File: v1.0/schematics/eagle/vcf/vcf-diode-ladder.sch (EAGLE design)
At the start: 42 parts, among them IC1 TL072P, J1 WAVE IN, J2 CUTOFF CV IN, J3 WAVE OUT, Q1 2N3417, Q2 2N3417, Q3 2N3417, Q4 2N3417, Q5 2N3906

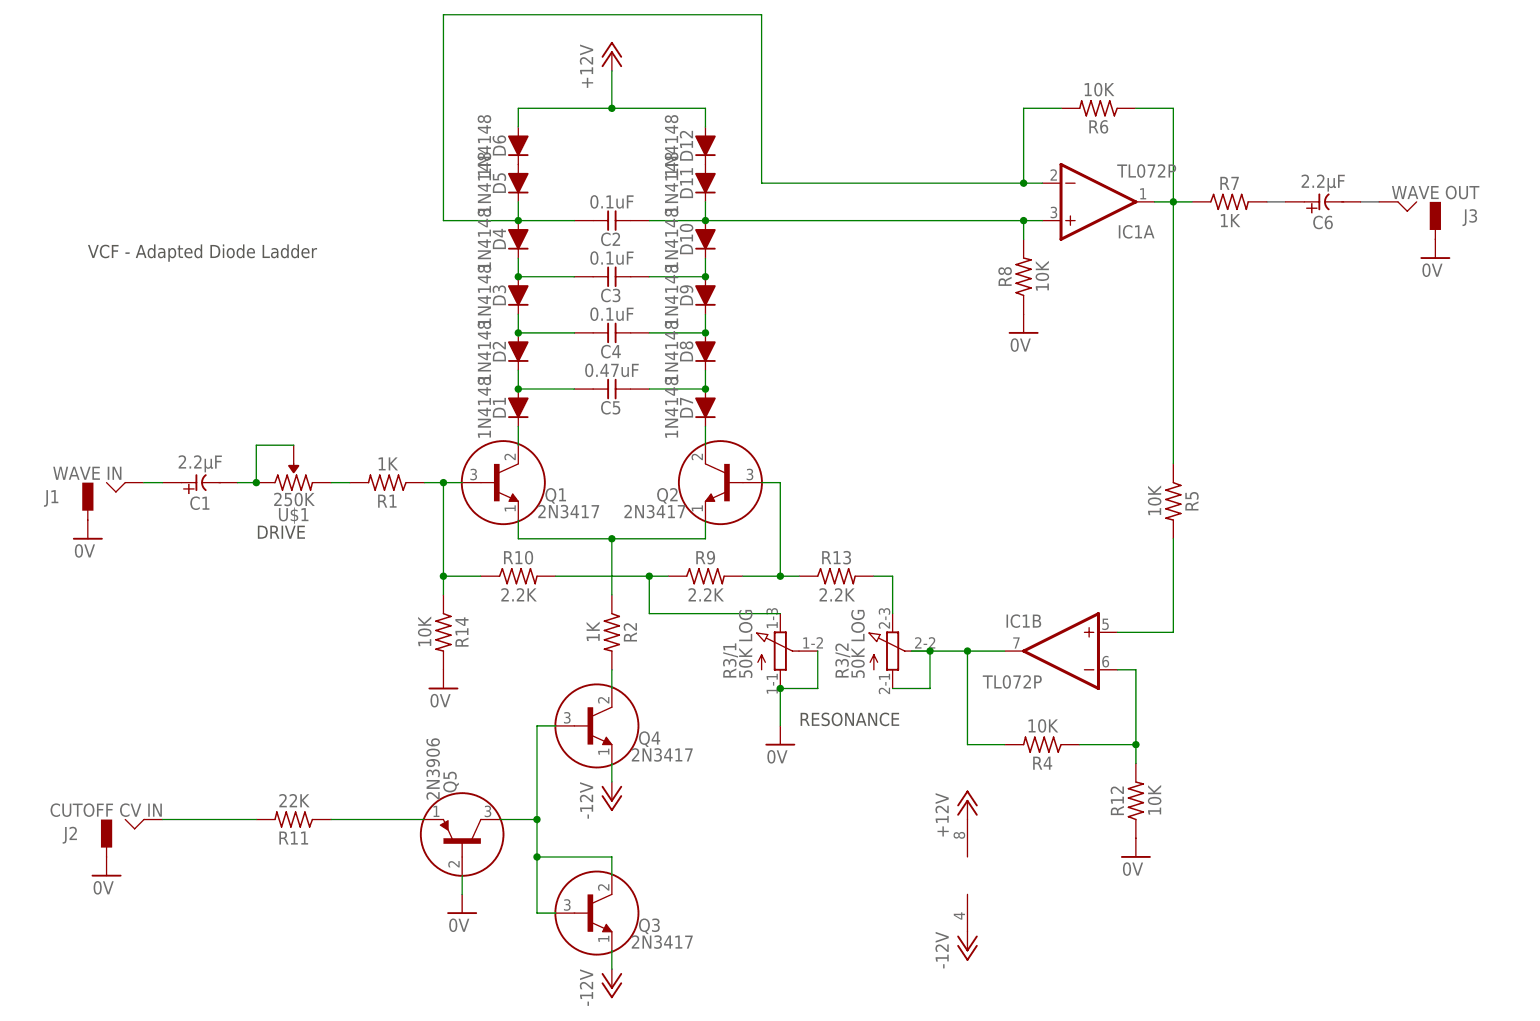
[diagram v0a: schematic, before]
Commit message: Updated vco with correct pot values Updated vcf with new values and added in manual CV control.
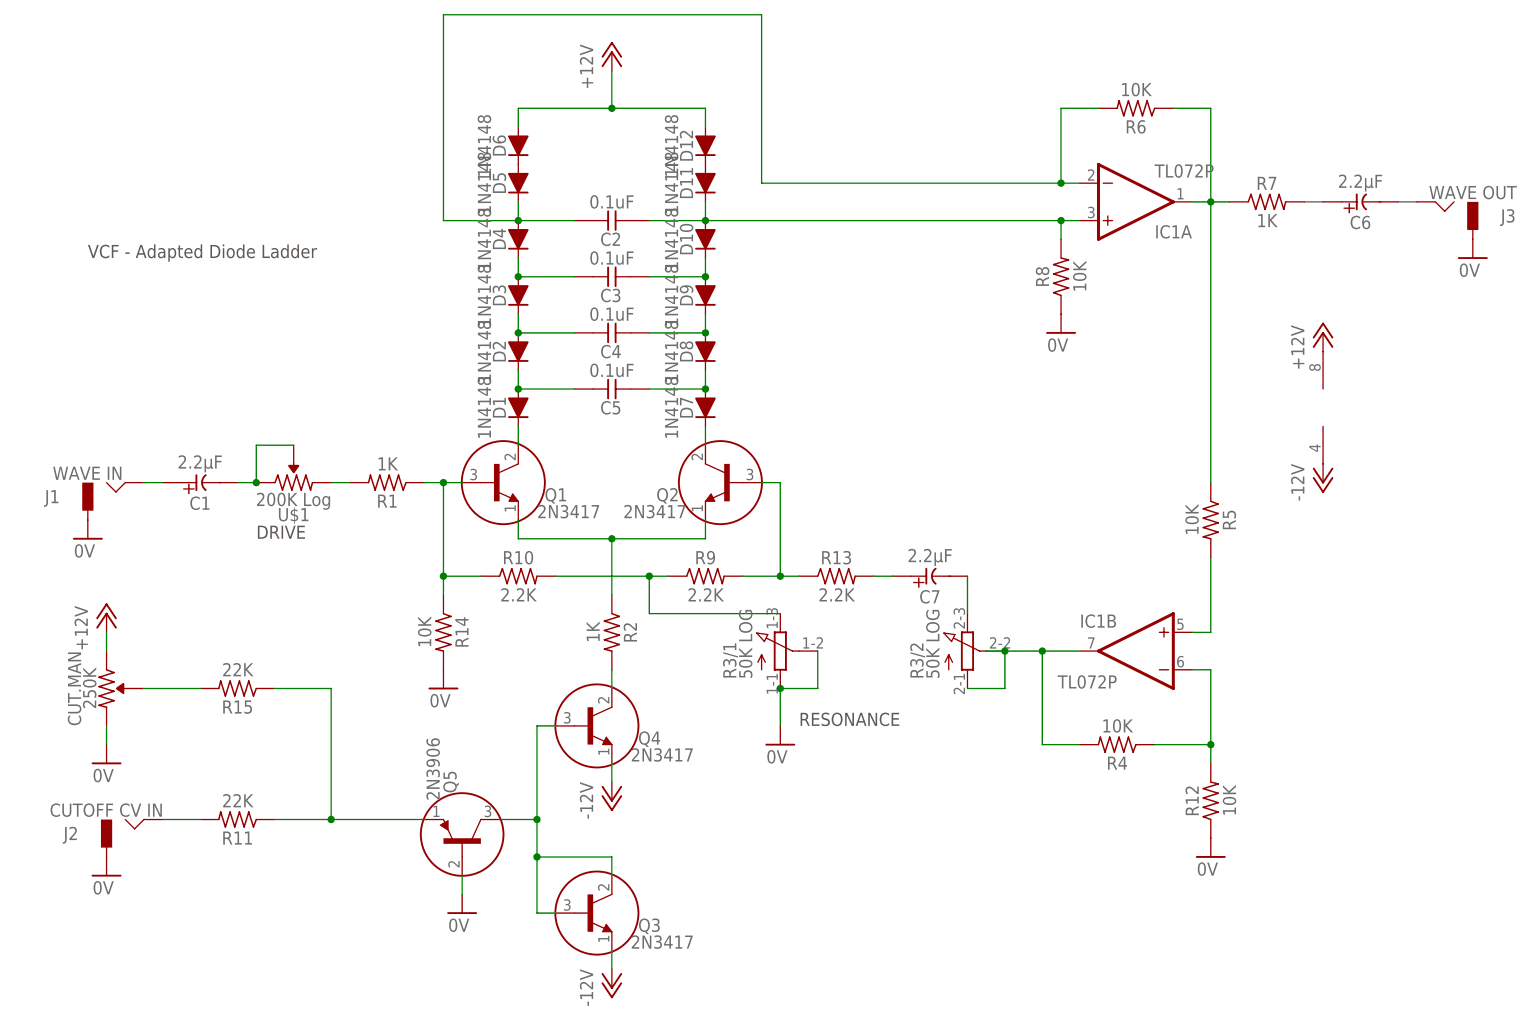
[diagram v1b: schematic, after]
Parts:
- added C7: 2.2μF, _common:CE-USE2-5
- added CUT.MAN: 250K, _common:R-VAR
- added R15: 22K, _common:R0309/10
- C5: value 0.47uF -> 0.1uF
- U$1: value 250K -> 200K Log
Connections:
- new net N$6: CUT.MAN.P$1, R15.2
- new net N$7: C7.-, R3/2.E
- net +12V: now also CUT.MAN.1
- net 0V: now also CUT.MAN.2
- net N$12: now also R15.1
- net N$18: now also C7.+; no longer R3/2.E
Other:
- moved on the sheet: C6, IC1A, IC1B, J3, R11, R12, R3/2, R4, R5, R6, R7, R8

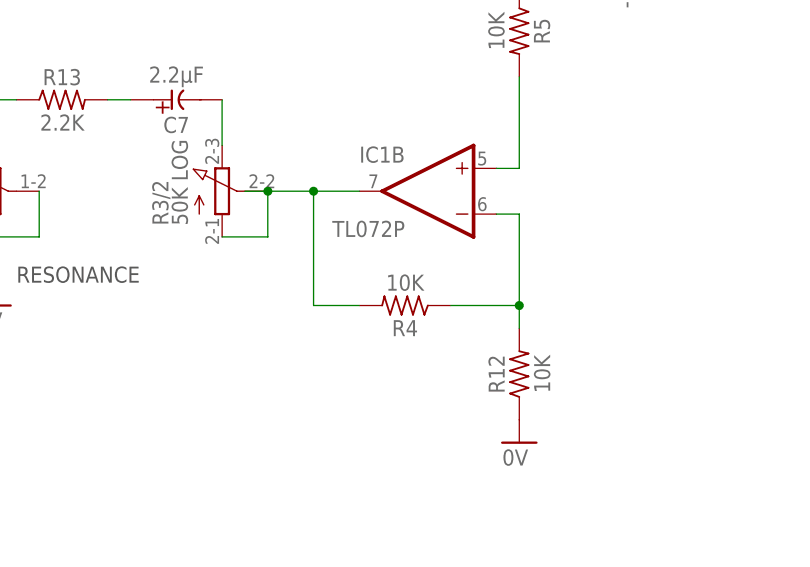
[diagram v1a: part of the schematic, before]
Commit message: updated vcf resonance amp r val
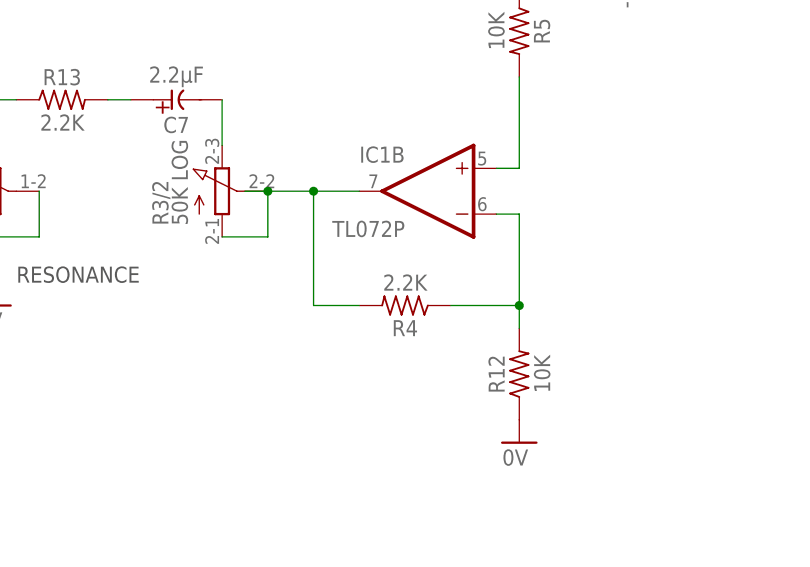
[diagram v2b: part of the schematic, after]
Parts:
- R4: value 10K -> 2.2K
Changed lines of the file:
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@@
 <part name="GND1" library="supply1" deviceset="0V" device=""/>
 <part name="R3" library="pot" deviceset="3RP/1610G" device="" value="50K LOG"/>
-<part name="R4" library="_common" deviceset="R" device="0309/10" value="10K"/>
+<part name="R4" library="_common" deviceset="R" device="0309/10" value="2.2K"/>
 <part name="R5" library="_common" deviceset="R" device="0309/10" value="10K"/>
 <part name="R12" library="_common" deviceset="R" device="0309/10" value="10K"/>

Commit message: Updated VCF
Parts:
- R4: value 2.2K -> 10K
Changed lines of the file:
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@@
 <part name="GND1" library="supply1" deviceset="0V" device=""/>
 <part name="R3" library="pot" deviceset="3RP/1610G" device="" value="50K LOG"/>
-<part name="R4" library="_common" deviceset="R" device="0309/10" value="2.2K"/>
+<part name="R4" library="_common" deviceset="R" device="0309/10" value="10K"/>
 <part name="R5" library="_common" deviceset="R" device="0309/10" value="10K"/>
 <part name="R12" library="_common" deviceset="R" device="0309/10" value="10K"/>

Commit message: Added VCF ATT
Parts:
- added ATT: 250K (lin), _common:R-VAR
- CUT.MAN: value 250K -> 250K (lin)
- R3: value 50K LOG -> 50K (log)
- U$1: value 200K Log -> 200K (log)
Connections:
- new net N$31: ATT.1, ATT.P$1, R11.2
- net N$4: now also ATT.2; no longer R11.2
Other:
- note added: "Updated: 2013-11-17"
- moved on the sheet: CUT.MAN, J2, R11, R15
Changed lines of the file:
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@@
 <part name="R2" library="_common" deviceset="R" device="0309/10" value="1K"/>
 <part name="GND1" library="supply1" deviceset="0V" device=""/>
-<part name="R3" library="pot" deviceset="3RP/1610G" device="" value="50K LOG"/>
+<part name="R3" library="pot" deviceset="3RP/1610G" device="" value="50K (log)"/>
 <part name="R4" library="_common" deviceset="R" device="0309/10" value="10K"/>
 <part name="R5" library="_common" deviceset="R" device="0309/10" value="10K"/>
@@
 <part name="R14" library="_common" deviceset="R" device="0309/10" value="10K"/>
 <part name="GND8" library="supply1" deviceset="0V" device=""/>
-<part name="U$1" library="_common" deviceset="R-VAR" device="" value="200K Log"/>
-<part name="CUT.MAN" library="_common" deviceset="R-VAR" device="" value="250K"/>
+<part name="U$1" library="_common" deviceset="R-VAR" device="" value="200K (log)"/>
+<part name="CUT.MAN" library="_common" deviceset="R-VAR" device="" value="250K (lin)"/>
 <part name="R15" library="_common" deviceset="R" device="0309/10" value="22K"/>
 <part name="P+3" library="supply1" deviceset="+12V" device=""/>
 <part name="GND9" library="supply1" deviceset="0V" device=""/>
 <part name="C7" library="_common" deviceset="CE-US" device="E2-5" value="2.2μF"/>
+<part name="ATT" library="_common" deviceset="R-VAR" device="" value="250K (lin)"/>
 </parts>
 <sheets>
 <sheet>
 <plain>
-<text x="43.18" y="58.42" size="1.778" layer="97">RESONANCE</text>
+<text x="55.88" y="58.42" size="1.778" layer="97">RESONANCE</text>
 <wire x1="111.76" y1="129.54" x2="114.3" y2="129.54" width="0.1524" layer="97"/>
 <wire x1="124.46" y1="129.54" x2="127" y2="129.54" width="0.1524" layer="97"/>
 <text x="-30.48" y="83.82" size="1.778" layer="97">DRIVE</text>
 <text x="-53.34" y="121.92" size="1.778" layer="97">VCF - Adapted Diode Ladder</text>
+<wire x1="45.72" y1="68.58" x2="53.34" y2="60.96" width="0.1524" layer="97" style="shortdash"/>
+<wire x1="53.34" y1="60.96" x2="76.2" y2="60.96" width="0.1524" layer="97" style="shortdash"/>
+<wire x1="76.2" y1="60.96" x2="68.58" y2="68.58" width="0.1524" layer="97" style="shortdash"/>
+<text x="-53.34" y="116.84" size="1.778" layer="97">Updated: 2013-11-17</text>
 </plain>
 <instances>
 <instance part="J1" gate="G$1" x="-50.8" y="88.9"/>
-<instance part="J2" gate="G$1" x="-48.26" y="43.18"/>
+<instance part="J2" gate="G$1" x="-50.8" y="43.18"/>
 <instance part="J3" gate="G$1" x="132.08" y="127" rot="MR0"/>
 <instance part="R1" gate="G$1" x="-12.7" y="91.44" rot="R180"/>
 <instance part="R6" gate="G$1" x="88.9" y="142.24" rot="R180"/>
 <instance part="R7" gate="G$1" x="106.68" y="129.54"/>
-<instance part="R11" gate="G$1" x="-33.02" y="45.72" rot="R180"/>
+<instance part="R11" gate="G$1" x="-20.32" y="45.72" rot="R180"/>
 <instance part="Q1" gate="G$1" x="2.54" y="91.44"/>
 <instance part="Q2" gate="G$1" x="33.02" y="91.44" rot="MR0"/>
@@
 <instance part="GND5" gate="1" x="-53.34" y="83.82"/>
 <instance part="GND6" gate="1" x="134.62" y="121.92"/>
-<instance part="GND7" gate="1" x="-50.8" y="38.1"/>
+<instance part="GND7" gate="1" x="-53.34" y="38.1"/>
 <instance part="C1" gate="G$1" x="-38.1" y="91.44" rot="R90"/>
 <instance part="IC1" gate="B" x="88.9" y="68.58" rot="MR0"/>
@@
 <instance part="GND8" gate="1" x="-5.08" y="63.5"/>
 <instance part="U$1" gate="G$1" x="-25.4" y="91.44"/>
-<instance part="CUT.MAN" gate="G$1" x="-50.8" y="63.5" rot="R270"/>
-<instance part="R15" gate="G$1" x="-33.02" y="63.5" rot="R180"/>
-<instance part="P+3" gate="1" x="-50.8" y="73.66"/>
-<instance part="GND9" gate="1" x="-50.8" y="53.34"/>
+<instance part="CUT.MAN" gate="G$1" x="-53.34" y="63.5" rot="R270"/>
+<instance part="R15" gate="G$1" x="-20.32" y="63.5" rot="R180"/>
+<instance part="P+3" gate="1" x="-53.34" y="73.66"/>
+<instance part="GND9" gate="1" x="-53.34" y="53.34"/>
 <instance part="C7" gate="G$1" x="60.96" y="78.74" rot="R90"/>
+<instance part="ATT" gate="G$1" x="-35.56" y="45.72" rot="R180"/>
 </instances>
 <busses>
 </busses>
 <nets>
-<net name="N$4" class="0">
-<segment>
-<pinref part="J2" gate="G$1" pin="HOT"/>
-<pinref part="R11" gate="G$1" pin="2"/>
-<wire x1="-38.1" y1="45.72" x2="-43.18" y2="45.72" width="0.1524" layer="91"/>
-</segment>
-</net>
 <net name="N$5" class="0">
 <segment>
@@
 <pinref part="R11" gate="G$1" pin="1"/>
 <pinref part="Q5" gate="G$1" pin="E"/>
-<wire x1="-27.94" y1="45.72" x2="-20.32" y2="45.72" width="0.1524" layer="91"/>
+<wire x1="-15.24" y1="45.72" x2="-12.7" y2="45.72" width="0.1524" layer="91"/>
 <pinref part="R15" gate="G$1" pin="1"/>
-<wire x1="-20.32" y1="45.72" x2="-7.62" y2="45.72" width="0.1524" layer="91"/>
-<wire x1="-27.94" y1="63.5" x2="-20.32" y2="63.5" width="0.1524" layer="91"/>
-<wire x1="-20.32" y1="63.5" x2="-20.32" y2="45.72" width="0.1524" layer="91"/>
-<junction x="-20.32" y="45.72"/>
+<wire x1="-12.7" y1="45.72" x2="-7.62" y2="45.72" width="0.1524" layer="91"/>
+<wire x1="-15.24" y1="63.5" x2="-12.7" y2="63.5" width="0.1524" layer="91"/>
+<wire x1="-12.7" y1="63.5" x2="-12.7" y2="45.72" width="0.1524" layer="91"/>
+<junction x="-12.7" y="45.72"/>
 </segment>
 </net>
@@
 <segment>
 <pinref part="CUT.MAN" gate="G$1" pin="2"/>
-<wire x1="-50.8" y1="55.88" x2="-50.8" y2="58.42" width="0.1524" layer="91"/>
+<wire x1="-53.34" y1="55.88" x2="-53.34" y2="58.42" width="0.1524" layer="91"/>
 <pinref part="GND9" gate="1" pin="0V"/>
 </segment>
@@
 <pinref part="CUT.MAN" gate="G$1" pin="1"/>
 <pinref part="P+3" gate="1" pin="+12V"/>
-<wire x1="-50.8" y1="71.12" x2="-50.8" y2="68.58" width="0.1524" layer="91"/>
+<wire x1="-53.34" y1="71.12" x2="-53.34" y2="68.58" width="0.1524" layer="91"/>
 </segment>
 </net>
@@
 <pinref part="CUT.MAN" gate="G$1" pin="P$1"/>
 <pinref part="R15" gate="G$1" pin="2"/>
-<wire x1="-45.72" y1="63.5" x2="-38.1" y2="63.5" width="0.1524" layer="91"/>
+<wire x1="-48.26" y1="63.5" x2="-25.4" y2="63.5" width="0.1524" layer="91"/>
 </segment>
 </net>
@@
 </segment>
 </net>
+<net name="N$4" class="0">
+<segment>
+<pinref part="J2" gate="G$1" pin="HOT"/>
+<pinref part="ATT" gate="G$1" pin="2"/>
+<wire x1="-45.72" y1="45.72" x2="-40.64" y2="45.72" width="0.1524" layer="91"/>
+</segment>
+</net>
+<net name="N$31" class="0">
+<segment>
+<pinref part="ATT" gate="G$1" pin="P$1"/>
+<wire x1="-35.56" y1="40.64" x2="-30.48" y2="40.64" width="0.1524" layer="91"/>
+<pinref part="ATT" gate="G$1" pin="1"/>
+<wire x1="-30.48" y1="40.64" x2="-30.48" y2="45.72" width="0.1524" layer="91"/>
+<pinref part="R11" gate="G$1" pin="2"/>
+<wire x1="-30.48" y1="45.72" x2="-25.4" y2="45.72" width="0.1524" layer="91"/>
+<junction x="-30.48" y="45.72"/>
+</segment>
+</net>
